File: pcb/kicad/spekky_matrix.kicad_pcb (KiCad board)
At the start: 2 copper layers, 153 x 95.8 mm, 330 parts, among them J1 USB_B_Micro, J2 Conn_ARM_JTAG_SWD_10, Q1 DMP3125L-7, Q2 DMP3125L-7, Q3 DMP3125L-7, Q4 DMP3125L-7, Q5 DMP3125L-7, Q6 DMP3125L-7, Q7 DMP3125L-7, Q8 DMP3125L-7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

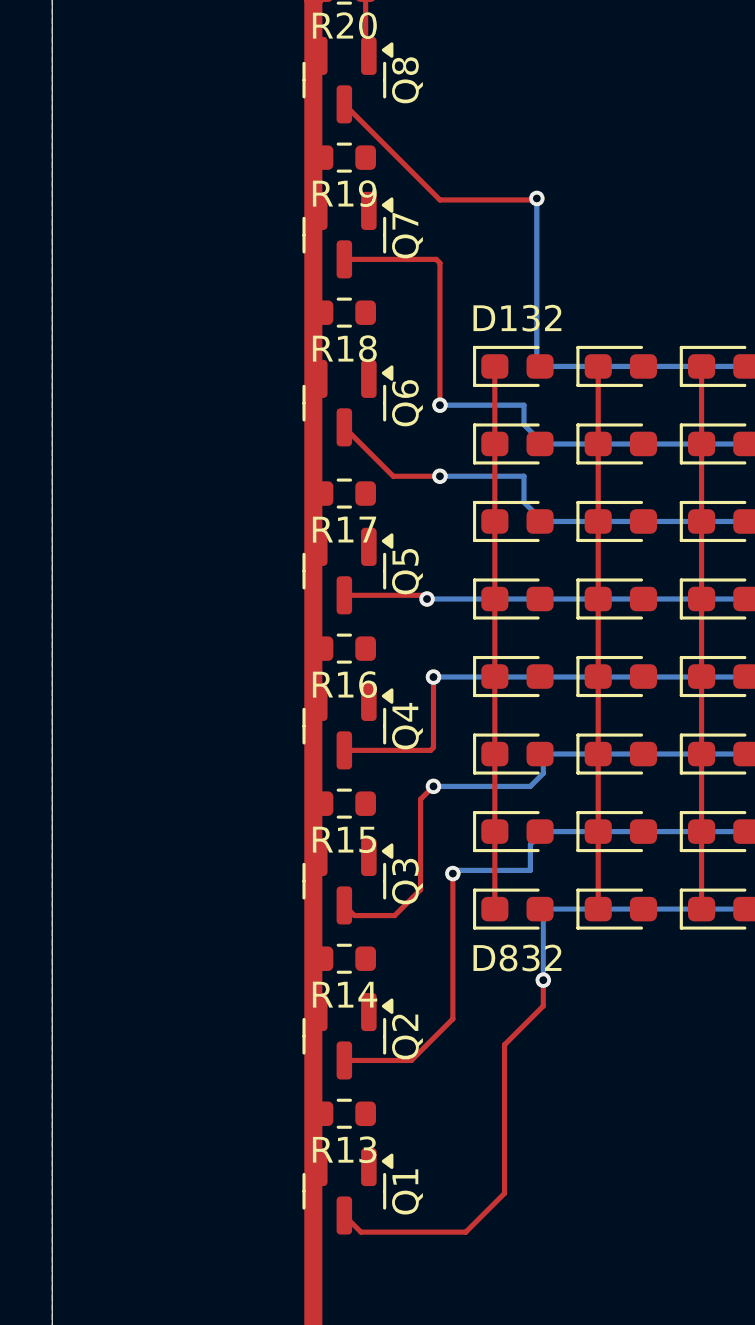
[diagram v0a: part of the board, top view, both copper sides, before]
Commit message: Connect mosfet gates to resistor
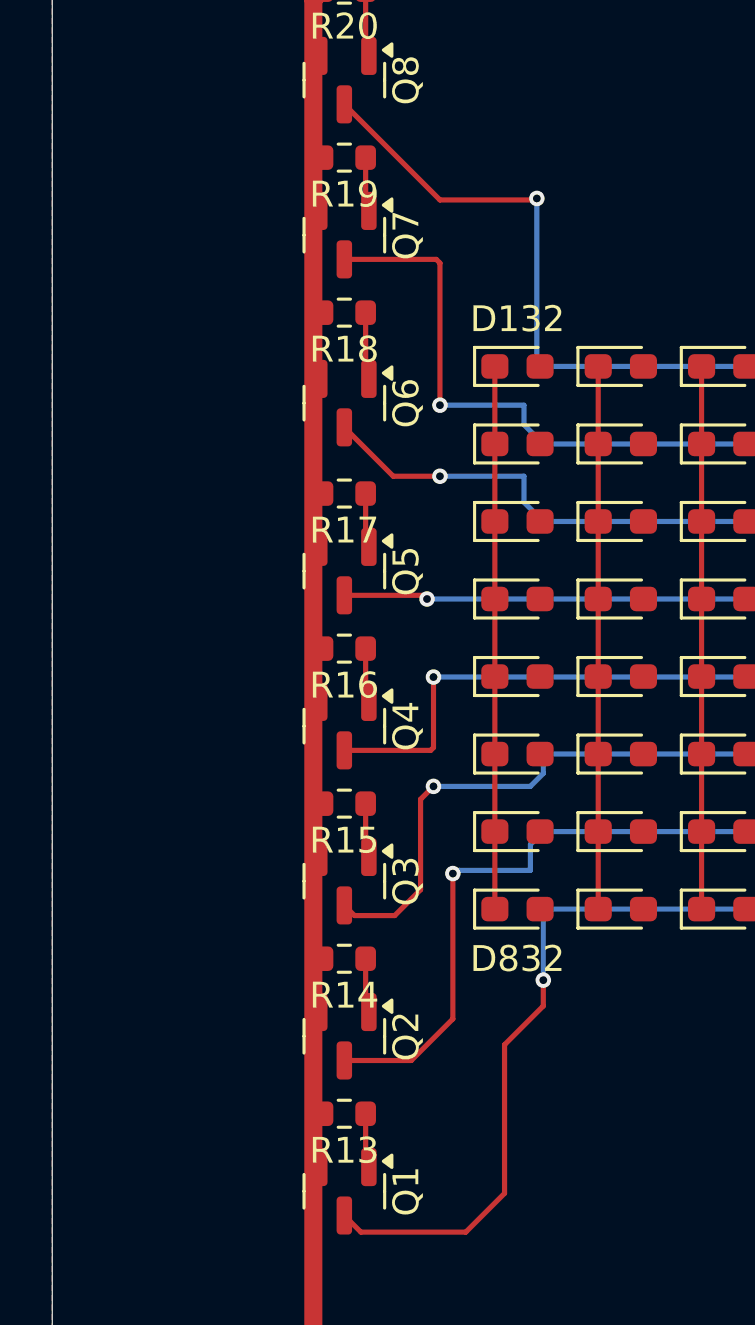
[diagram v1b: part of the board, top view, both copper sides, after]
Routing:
- net Net-(Q6-G): track 0.00 -> 2.61 mm
- net Net-(Q7-G): track 0.00 -> 2.11 mm
- net Net-(Q5-G): track 0.00 -> 2.11 mm
- net Net-(Q4-G): track 0.00 -> 2.11 mm
- net Net-(Q3-G): track 0.00 -> 2.11 mm
- net Net-(Q2-G): track 0.00 -> 2.11 mm
- net Net-(Q1-G): track 0.00 -> 2.11 mm
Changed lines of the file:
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@@
+	)
+	(segment
+		(start 67.125 92.8575)
+		(end 67.25 92.9825)
+		(width 0.2)
+		(layer "F.Cu")
+		(net 60)
+	)
+	(segment
+		(start 67.125 90.92)
+		(end 67.125 92.8575)
+		(width 0.2)
+		(layer "F.Cu")
+		(net 60)
+	)
+	(segment
+		(start 67.125 86.8575)
+		(end 67.25 86.9825)
+		(width 0.2)
+		(layer "F.Cu")
+		(net 61)
+	)
+	(segment
+		(start 67.125 84.92)
+		(end 67.125 86.8575)
+		(width 0.2)
+		(layer "F.Cu")
+		(net 61)
+	)
+	(segment
+		(start 67.125 80.8575)
+		(end 67.25 80.9825)
+		(width 0.2)
+		(layer "F.Cu")
+		(net 62)
+	)
+	(segment
+		(start 67.125 78.92)
+		(end 67.125 80.8575)
+		(width 0.2)
+		(layer "F.Cu")
+		(net 62)
+	)
+	(segment
+		(start 67.125 74.8575)
+		(end 67.25 74.9825)
+		(width 0.2)
+		(layer "F.Cu")
+		(net 63)
+	)
+	(segment
+		(start 67.125 72.92)
+		(end 67.125 74.8575)
+		(width 0.2)
+		(layer "F.Cu")
+		(net 63)
+	)
+	(segment
+		(start 67.125 68.8575)
+		(end 67.25 68.9825)
+		(width 0.2)
+		(layer "F.Cu")
+		(net 64)
+	)
+	(segment
+		(start 67.125 66.92)
+		(end 67.125 68.8575)
+		(width 0.2)
+		(layer "F.Cu")
+		(net 64)
+	)
+	(segment
+		(start 67.125 59.92)
+		(end 67.125 62.3575)
+		(width 0.2)
+		(layer "F.Cu")
+		(net 65)
+	)
+	(segment
+		(start 67.125 62.3575)
+		(end 67.25 62.4825)
+		(width 0.2)
+		(layer "F.Cu")
+		(net 65)
+	)
+	(segment
+		(start 67.125 55.8575)
+		(end 67.25 55.9825)
+		(width 0.2)
+		(layer "F.Cu")
+		(net 66)
+	)
+	(segment
+		(start 67.125 53.92)
+		(end 67.125 55.8575)
+		(width 0.2)
+		(layer "F.Cu")
+		(net 66)
 	)
 	(segment

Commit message: Add i2s traces
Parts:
- moved R2 4.15 mm to (108.5, 98.8), turned to 0 degrees
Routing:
- net /I2S MIC/I2S_SD: track 0.00 -> 27.3 mm, vias 0 -> 2
- net /I2S MIC/I2S_SCK: track 0.00 -> 19.2 mm, vias 0 -> 2
- net /I2S MIC/I2S_WS: track 0.00 -> 11.5 mm, vias 0 -> 2

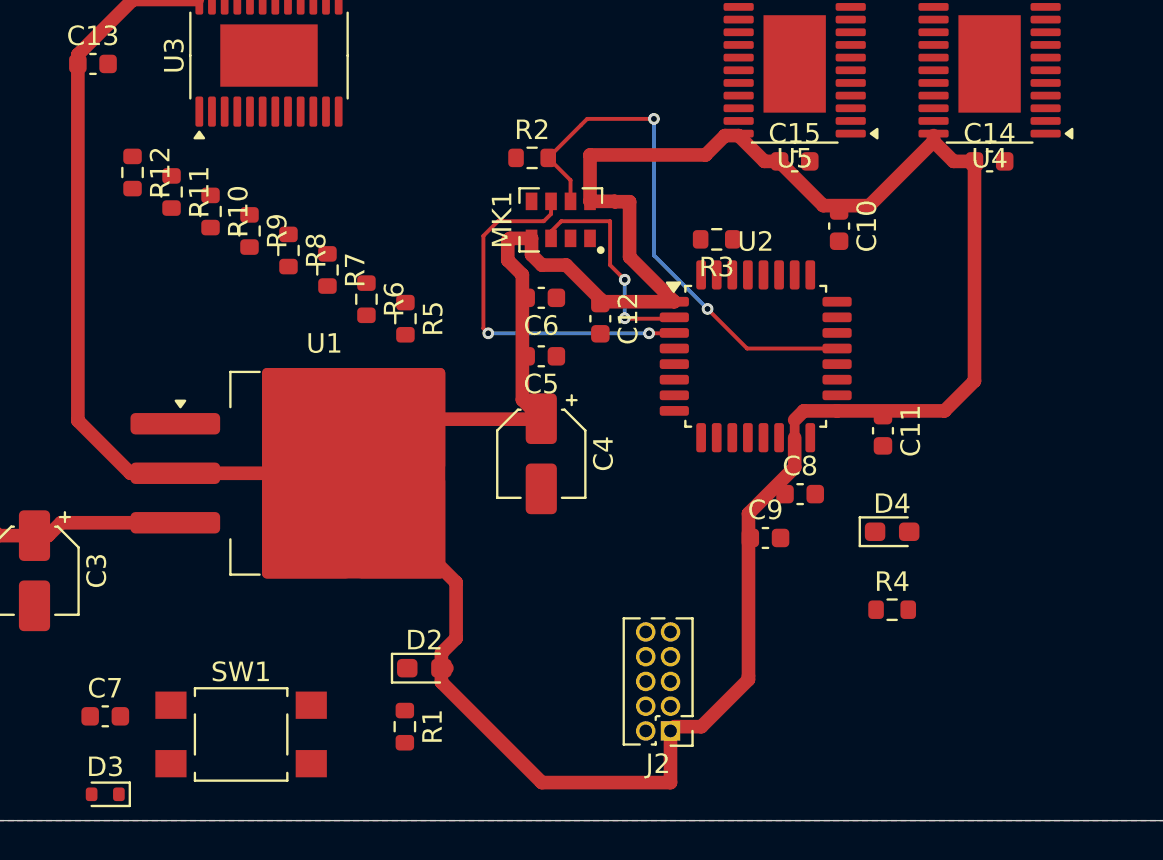
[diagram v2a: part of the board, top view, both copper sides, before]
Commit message: Connect arm swd connector
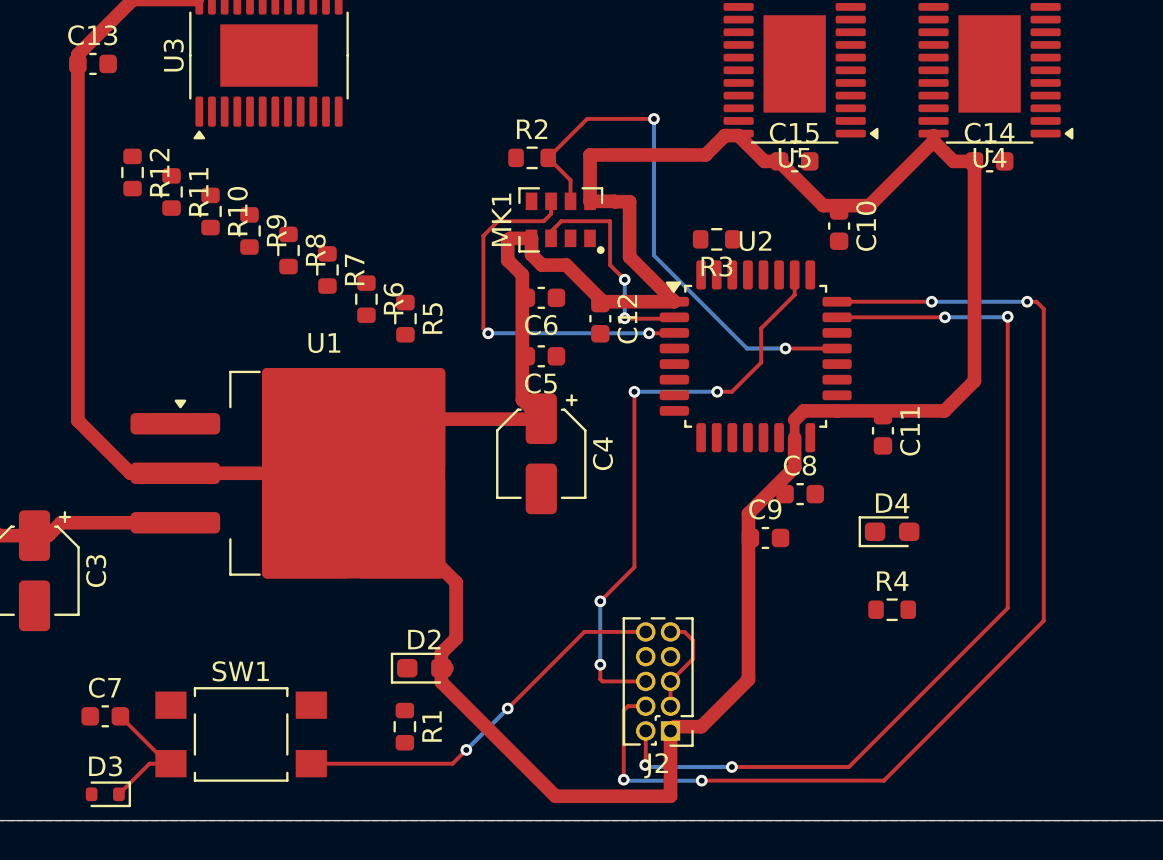
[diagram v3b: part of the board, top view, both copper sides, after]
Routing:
- net /STM32 MCU/SWD_SWCLK: track 0.00 -> 56.5 mm, vias 0 -> 4
- net /STM32 MCU/SWD_SWDIO: track 0.00 -> 47.6 mm, vias 0 -> 4
- net /LED DRIVING/SPI_CLK: track 0.00 -> 30.2 mm, vias 0 -> 4
- net /STM32 MCU/NRST: track 0.00 -> 26.9 mm, vias 0 -> 2
- net GND: track 0.00 -> 5.18 mm
- net +3V3: track 169.3 -> 170.3 mm

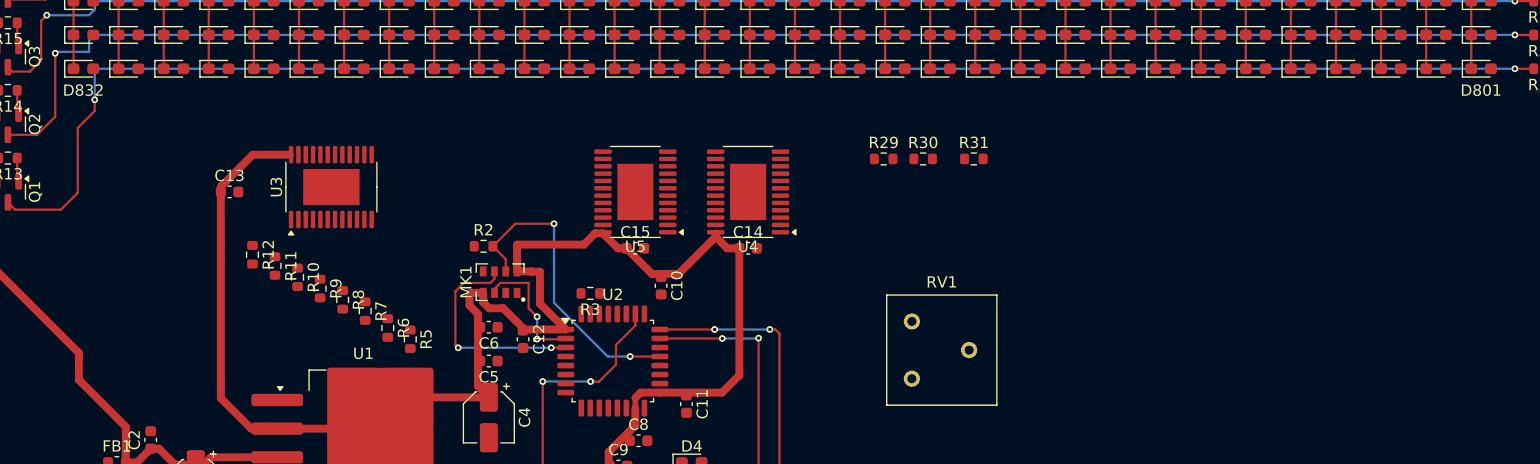
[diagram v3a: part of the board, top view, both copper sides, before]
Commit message: Connect col traces for led matrix
- Needed to move U4 (1x LED driver IC), increasing the distance between
  U4 and U3 (2x LED driver ICs)
- Also needed to alter the 3V3 trace too for the decoupling cap and U4
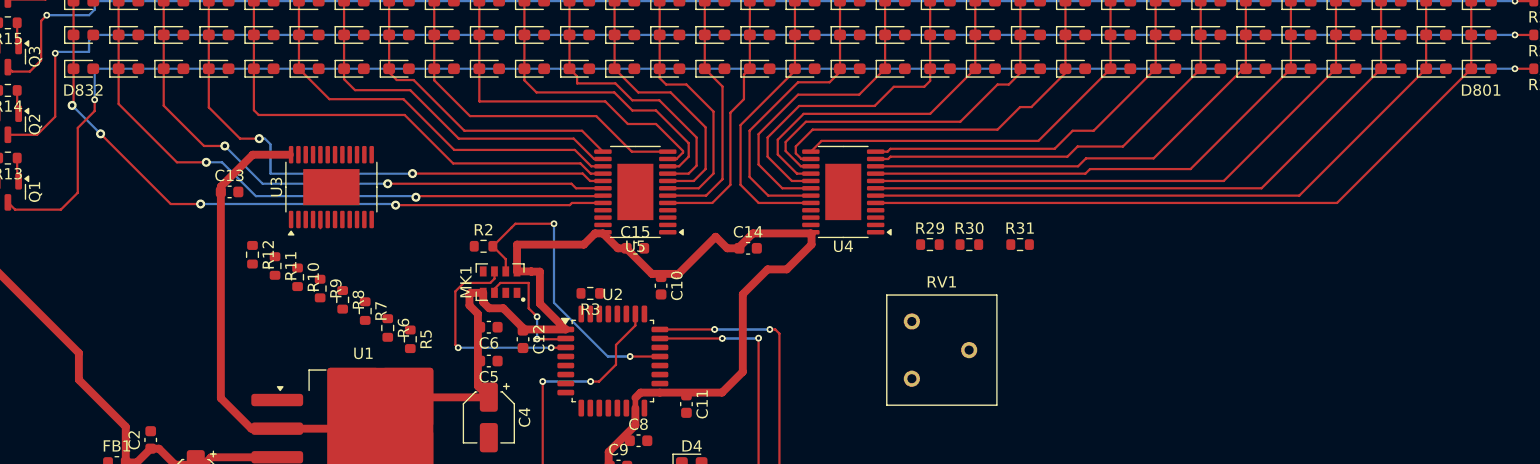
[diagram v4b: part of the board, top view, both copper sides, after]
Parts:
- moved R29 8.64 mm to (148.1, 98.6)
- moved R30 8.64 mm to (151.6, 98.6)
- moved R31 8.64 mm to (156.1, 98.6)
- moved U4 8.44 mm to (140.4, 93.9)
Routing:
- net /LED DRIVING/COL1: track 21.0 -> 78.8 mm
- net /LED DRIVING/COL32: track 21.0 -> 75.1 mm, vias 0 -> 4
- net /LED DRIVING/COL2: track 21.0 -> 74.5 mm
- net /LED DRIVING/COL31: track 21.0 -> 70.6 mm, vias 0 -> 2
- net /LED DRIVING/COL3: track 21.0 -> 70.2 mm
- net /LED DRIVING/COL30: track 21.0 -> 66.3 mm, vias 0 -> 2
- net /LED DRIVING/COL4: track 21.0 -> 66.0 mm
- net /LED DRIVING/COL29: track 21.0 -> 63.6 mm, vias 0 -> 2
- net /LED DRIVING/COL5: track 21.0 -> 61.7 mm
- net /LED DRIVING/COL28: track 21.0 -> 58.0 mm
- net /LED DRIVING/COL6: track 21.0 -> 57.4 mm
- net /LED DRIVING/COL7: track 21.0 -> 53.2 mm
- net /LED DRIVING/COL27: track 21.0 -> 51.6 mm
- net /LED DRIVING/COL9: track 21.0 -> 50.6 mm
- net /LED DRIVING/COL10: track 21.0 -> 50.1 mm
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
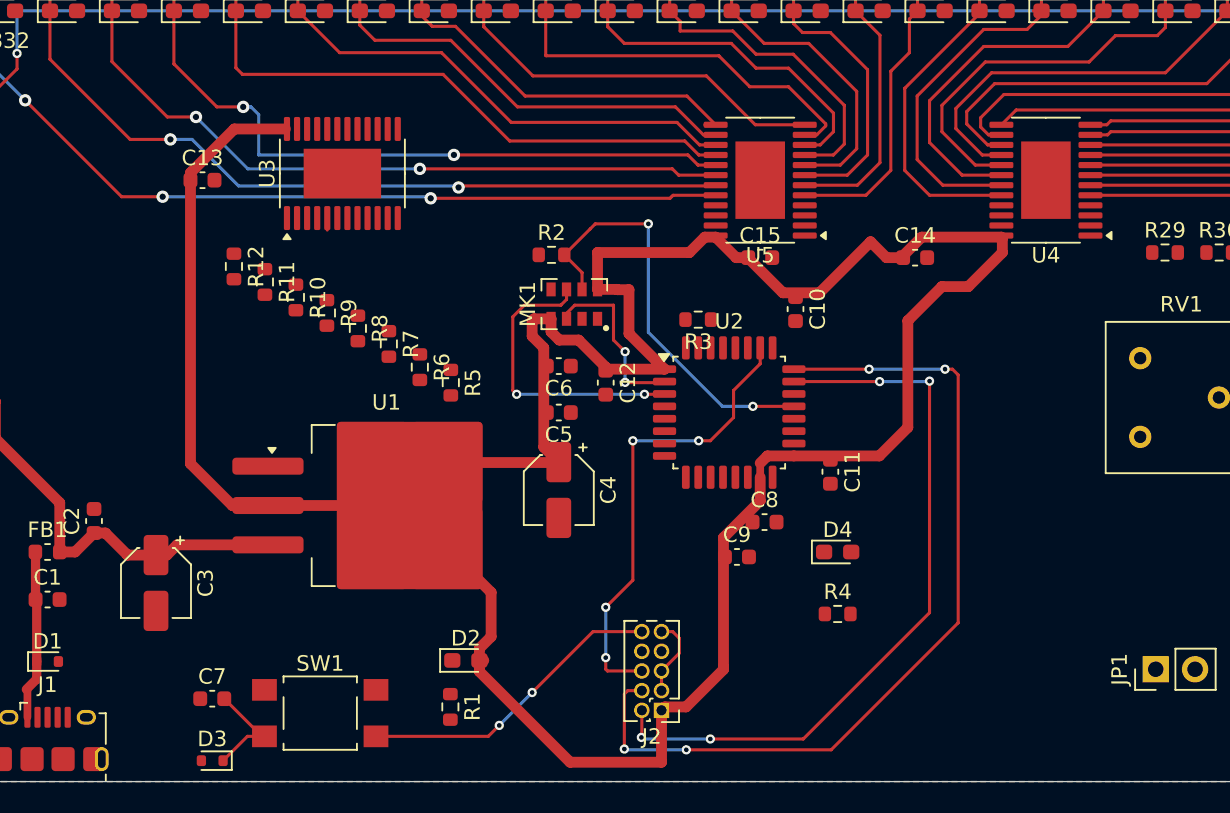
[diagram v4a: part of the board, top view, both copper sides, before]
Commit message: Connect spi traces
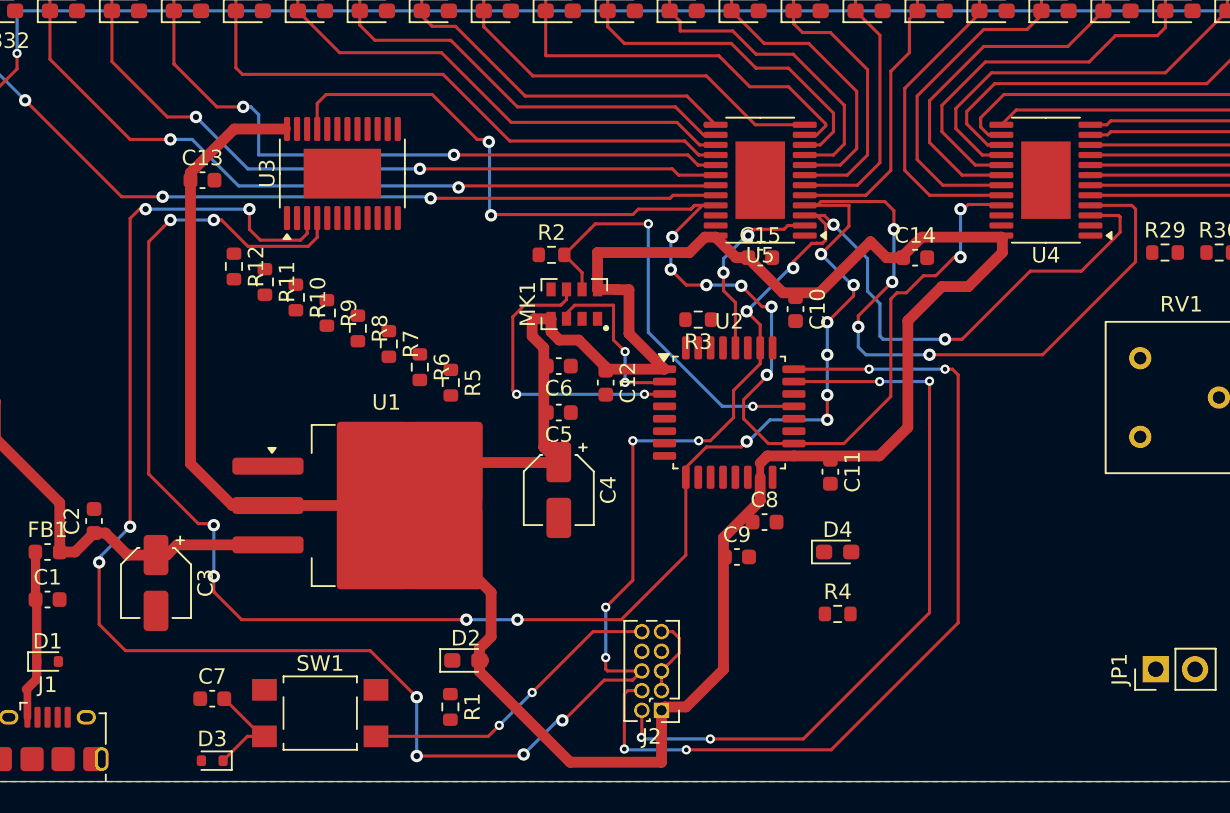
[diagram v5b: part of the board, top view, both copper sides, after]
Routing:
- net /LED DRIVING/GPIO_LE: track 0.00 -> 149.7 mm, vias 0 -> 17
- net /LED DRIVING/SPI_CLK: track 30.2 -> 159.2 mm, vias 4 -> 16
- net /LED DRIVING/SPI_OE: track 0.00 -> 84.6 mm, vias 0 -> 10
- net /LED DRIVING/SPI_MOSI: track 0.00 -> 12.2 mm, vias 0 -> 2
- net /LED DRIVING/~{OUT0}: track 0.77 -> 0.00 mm
